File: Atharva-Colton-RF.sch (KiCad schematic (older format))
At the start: 17 parts

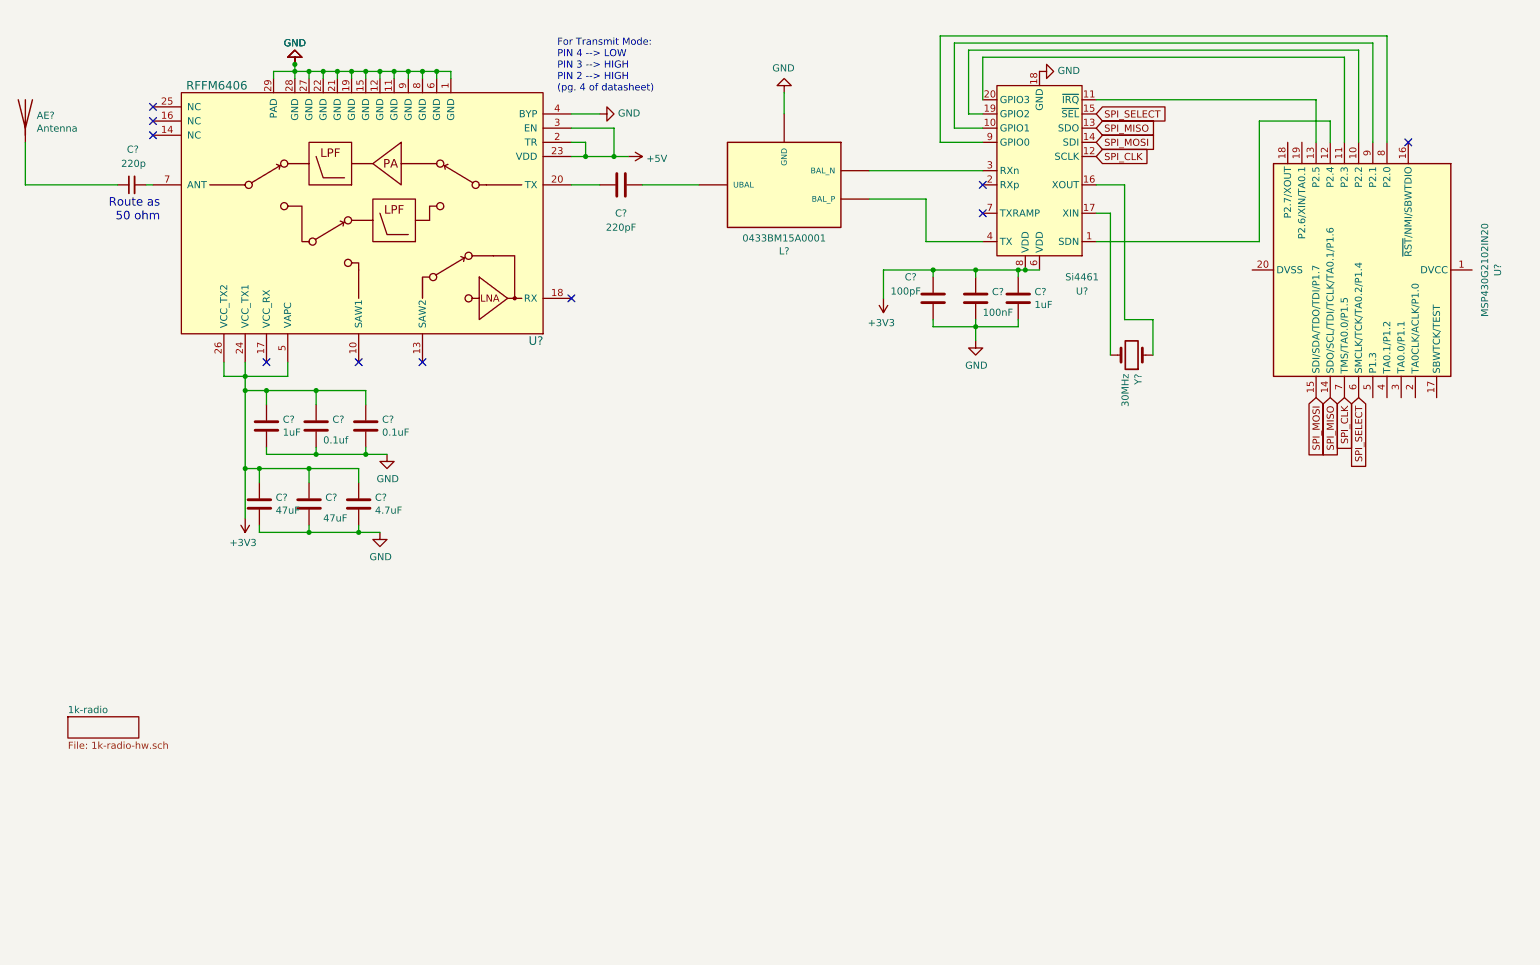
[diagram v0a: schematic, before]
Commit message: RX design in schematic
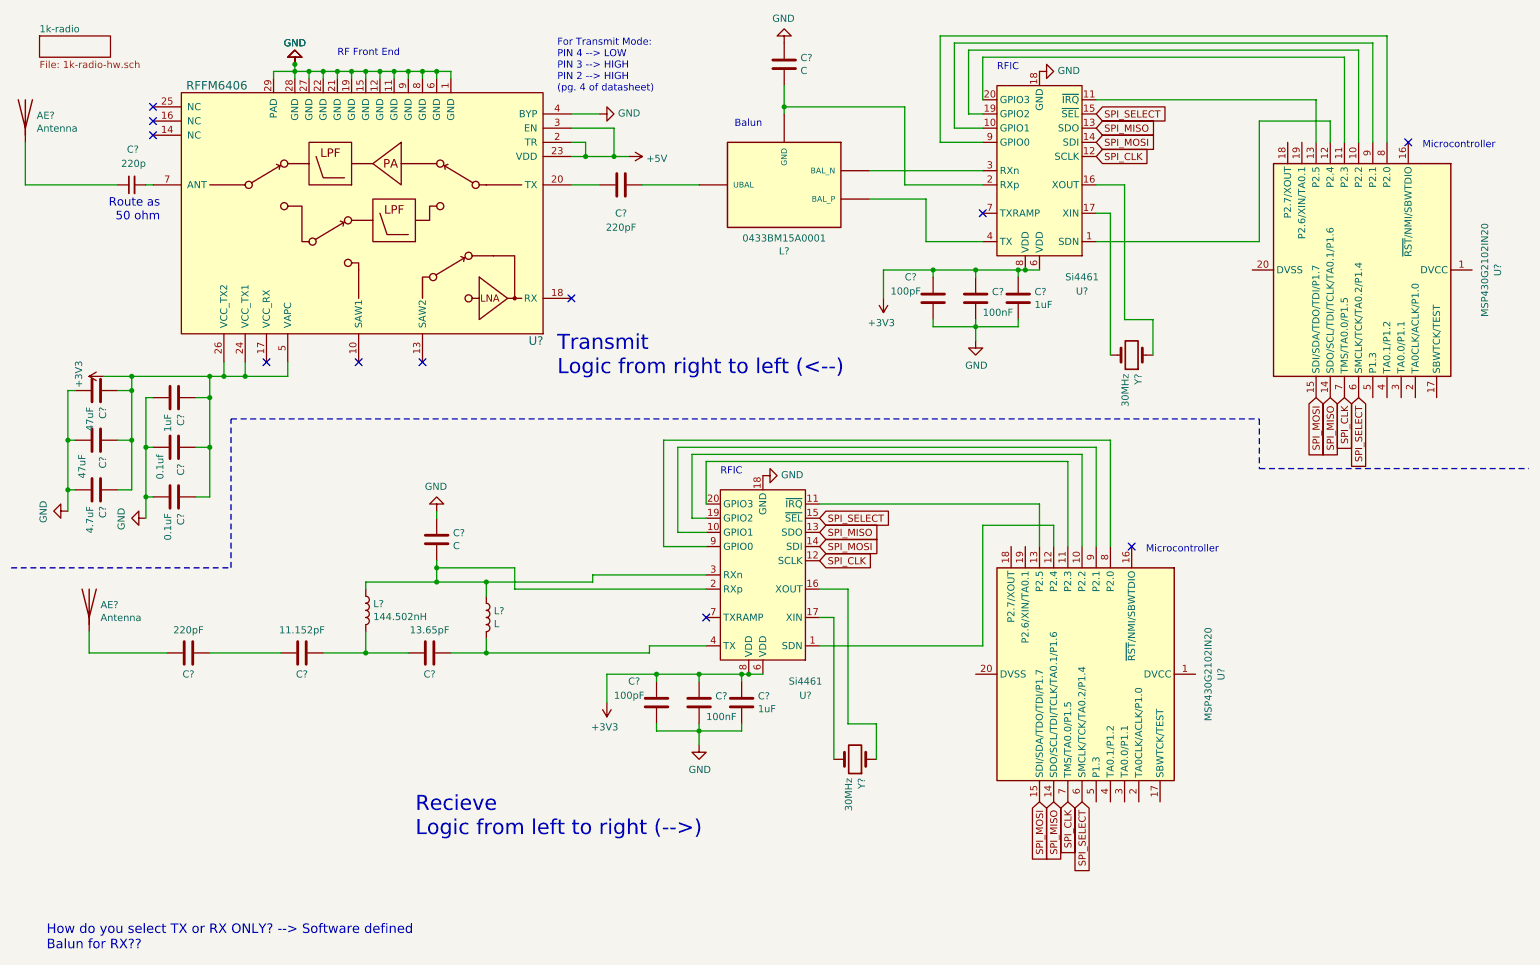
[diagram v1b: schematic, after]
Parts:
- added AE?: Antenna, symbol Device:Antenna
- added C?: 220pF, symbol Device:C
- added C?: 11.152pF, symbol Device:C
- added C?: 13.65pF, symbol Device:C
- added C?: 100nF, symbol Device:C
- added C?: 1uF, symbol Device:C
- added C?: 100pF, symbol Device:C
- added C? (x2): C, symbol Device:C
- added L?: 144.502nH, symbol Device:L
- added L?: L, symbol Device:L
- added U?: Si4461, Package_DFN_QFN:QFN-20-1EP_4x4mm_P0.5mm_EP2.6x2.6mm_ThermalVias, symbol RF:Si4461
- added U?: MSP430G2102IN20, Package_DIP:DIP-20_W7.62mm, symbol MCU_Texas_MSP430:MSP430G2102IN20
- added Y?: 30MHz, symbol Device:Crystal
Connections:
- net +3V3: now also C?.1, C?.1, C?.1, U?.6 (VDD), U?.8 (VDD)
- net GND: now also C?.1, C?.1, C?.2, C?.2, C?.2, U?.18 (GND), U?.21 (GND); no longer L?.2 (GND), L?.5 (GND), L?.6 (GND)
- net SPI_CLK: now also U?.12 (SCLK), U?.7 (TMS/TA0.0/P1.5)
- net SPI_MISO: now also U?.13 (SDO), U?.14 (SDO/SCL/TDI/TCLK/TA0.1/P1.6)
- net SPI_MOSI: now also U?.14 (SDI), U?.15 (SDI/SDA/TDO/TDI/P1.7)
- net SPI_SELECT: now also U?.15 (~SEL), U?.6 (SMCLK/TCK/TA0.2/P1.4)
- net at U?.2 (RXp): now also L?.2 (GND), L?.5 (GND), L?.6 (GND), C?.2
- new net: AE?.1 (A), C?.1
- new net: C?.2, C?.2
- new net: C?.1, C?.2, L?.2
- new net: C?.1, L?.2, U?.4 (TX)
- new net: C?.2, L?.1, L?.1, U?.2 (RXp), U?.3 (RXn)
- new net: U?.1 (SDN), U?.12 (P2.4)
- new net: U?.10 (GPIO1), U?.9 (P2.1)
- new net: U?.11 (~IRQ), U?.13 (P2.5)
- new net: U?.16 (XOUT), Y?.1
- new net: U?.17 (XIN), Y?.2
- new net: U?.10 (P2.2), U?.19 (GPIO2)
- new net: U?.11 (P2.3), U?.20 (GPIO3)
- new net: U?.8 (P2.0), U?.9 (GPIO0)
- no-connect marks 10 -> 11
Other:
- note added: "Balun\n"
- note added: "How do you select TX or RX ONLY? --> Software defined\nBalun for RX??\n"
- note added: "Microcontroller\n"
- note added: "RF Front End"
- note added: "RFIC"
- note added: "Recieve\nLogic from left to right (-->)"
- note added: "Transmit\nLogic from right to left (<--)"
- moved on the sheet: C?
